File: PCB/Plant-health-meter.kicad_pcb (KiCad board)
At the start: 4 copper layers, 128 x 25 mm, 85 parts, among them J1 Conn_01x02, J2 Conn_01x02, J3 Conn_01x04, J4 UJ2-MIBH2-4-SMT-TR, J5 Conn_01x02, Q1 AO3401A, SW1 Boot, SW2 Reset, U1 LTC4412xS6, U2 TPS62172DSG, U3 USBLC6-2P6, U4 ESP32-C3FH4X, U5 BME280, U6 TPS61022, U8 TP4057, U9 TLC555xD, Y1 40MHz

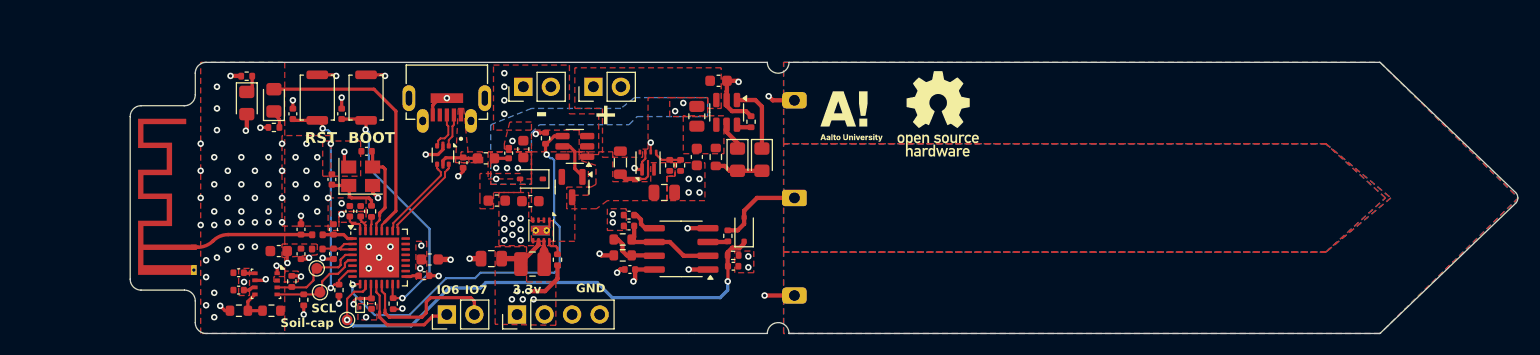
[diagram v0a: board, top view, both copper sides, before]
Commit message: Added light sensor simulation and schematic
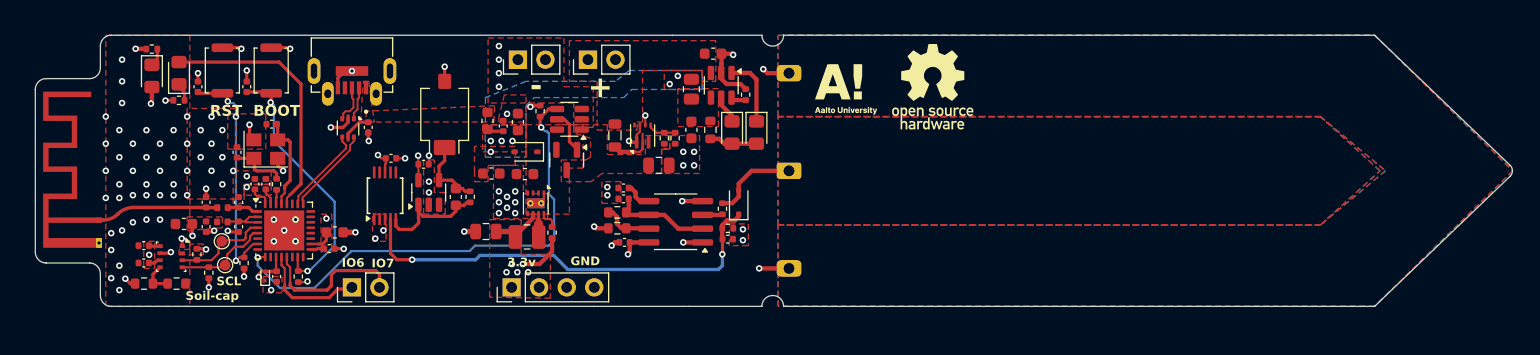
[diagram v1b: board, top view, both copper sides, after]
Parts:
- removed TP3: TestPoint, TestPoint:TestPoint_Pad_D1.0mm
- added C1: 100n, Capacitor_SMD:C_0402_1005Metric, F.Cu at (118.0, 108.8)
- added C30: 1u, Capacitor_SMD:C_0603_1608Metric, F.Cu at (124.0, 112.4)
- added C31: 100n, Capacitor_SMD:C_0402_1005Metric, F.Cu at (121.0, 109.4)
- added D7: BPW34-SMD, OptoDevice:Osram_BPW34S-SMD, F.Cu at (123.0, 104.8)
- added R21: 33k, Resistor_SMD:R_0402_1005Metric, F.Cu at (125.3, 112.4)
- added U12: ADS1115IDGS, Package_SO:TSSOP-10_3x3mm_P0.5mm, F.Cu at (117.5, 112.3)
- added U7: OPA340NA, Package_TO_SOT_SMD:SOT-23-5, F.Cu at (121.5, 112.0)
- moved C3 9.33 mm to (116.0, 106.0)
- moved AE1 9.10 mm to (91.1, 114.5)
- moved C10 9.10 mm to (99.0, 114.9)
- moved C11 9.10 mm to (101.0, 115.2)
- moved C12 9.10 mm to (104.0, 115.2)
- moved C13 9.10 mm to (112.3, 117.2)
- moved C14 9.10 mm to (112.9, 115.7)
- moved C15 9.10 mm to (104.0, 112.9)
- moved C16 9.10 mm to (107.5, 119.8)
- moved C17 9.10 mm to (101.0, 112.9)
- moved C18 9.10 mm to (105.5, 111.2)
- moved C19 9.10 mm to (106.5, 111.2)
- moved C20 9.10 mm to (100.2, 102.2)
- moved C21 9.10 mm to (95.2, 118.5)
- moved C22 9.10 mm to (95.2, 116.9)
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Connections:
- C26 pad 2: /MCU/Soil_cap -> /ADC/Soil_cap
- D8 pad 1: /MCU/Soil_cap -> /ADC/Soil_cap
- R17 pad 2: /MCU/Soil_cap -> /ADC/Soil_cap
- U4 pad 10: /MCU/Soil_cap -> unconnected-(U4-MTDI-Pad10)
- U4 pad 18: unconnected-(U4-VDD_SPI-Pad18) -> +3.3V
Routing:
- net /MCU/Soil_cap: track 47.9 -> 0.00 mm, vias 2 -> 0
- net /ADC/Soil_cap: track 0.00 -> 40.7 mm, vias 0 -> 2
- net /ADC/Light level: track 0.00 -> 11.2 mm
- net /MCU/Battery_stat: track 37.2 -> 45.4 mm
- net +3.3V: track 37.0 -> 43.8 mm, vias 22 -> 23
- net Net-(D7-K): track 0.00 -> 6.76 mm
- net GND: track 41.1 -> 44.0 mm, vias 101 -> 108
- net VBUS: track 3.72 -> 2.71 mm
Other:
- board size 128 x 25 mm -> 136.2 x 25 mm

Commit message: Light sensor
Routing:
- net Net-(D7-K): track 6.76 -> 4.82 mm
- net GND: track 44.0 -> 42.6 mm, vias 108 -> 107
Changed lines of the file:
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@@
 			(outputformat 1)
 			(mirror no)
-			(drillshape 1)
+			(drillshape 0)
 			(scaleselection 1)
-			(outputdirectory "")
+			(outputdirectory "manufacture/")
 		)
 	)
@@
 		(tags "capacitor")
 		(property "Reference" "C31"
-			(at 0 -1.16 360)
+			(at 0 -1.16 0)
 			(layer "F.SilkS")
 			(hide yes)
@@
 		)
 		(property "Value" "100n"
-			(at 0 1.16 360)
+			(at 0 1.16 0)
 			(layer "F.Fab")
 			(effects
@@
 		)
 		(fp_text user "${REFERENCE}"
-			(at 0 0 360)
+			(at 0 0 0)
 			(layer "F.Fab")
 			(effects
@@
 		(tags "capacitor")
 		(property "Reference" "C1"
-			(at 0 -1.16 360)
+			(at 0 -1.16 0)
 			(layer "F.SilkS")
 			(hide yes)
@@
 		)
 		(property "Value" "100n"
-			(at 0 1.16 360)
+			(at 0 1.16 0)
 			(layer "F.Fab")
 			(effects
@@
 		)
 		(fp_text user "${REFERENCE}"
-			(at 0 0 360)
+			(at 0 0 0)
 			(layer "F.Fab")
 			(effects
@@
 	)
 	(segment
-		(start 123 101.75)
-		(end 123 100.4)
-		(width 0.3)
-		(layer "F.Cu")
-		(net 2)
-	)
-	(segment
 		(start 115.95 106.48)
 		(end 115.95 107.2)
@@
 	)
 	(via
-		(at 123 100.4)
-		(size 0.6)
-		(drill 0.3)
-		(layers "F.Cu" "B.Cu")
-		(net 2)
-	)
-	(via
 		(at 91.75 110)
 		(size 0.6)
@@
 	)
 	(segment
-		(start 122.479999 109.57)
-		(end 123 109.049999)
-		(width 0.3)
-		(layer "F.Cu")
-		(net 57)
-	)
-	(segment
 		(start 124.6325 111.6325)
 		(end 124.029999 111.6325)
@@
 		(width 0.3)
 		(layer "F.Cu")
-		(net 57)
-	)
-	(segment
-		(start 123 109.049999)
-		(end 123 107.85)
-		(width 0.3)
-		(layer "F.Cu")

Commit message: Cleaned up
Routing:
- net Net-(D7-K): track 4.82 -> 6.76 mm
- net GND: track 42.6 -> 44.1 mm, vias 107 -> 108
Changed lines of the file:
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@@
 	)
 	(segment
+		(start 123 101.75)
+		(end 123 100.25)
+		(width 0.3)
+		(layer "F.Cu")
+		(net 2)
+	)
+	(segment
 		(start 138.69 116.6)
 		(end 138.3975 116.8925)
@@
 	)
 	(via
+		(at 123 100.25)
+		(size 0.6)
+		(drill 0.3)
+		(layers "F.Cu" "B.Cu")
+		(net 2)
+	)
+	(via
 		(at 94.5 98.75)
 		(size 0.6)
@@
 	)
 	(segment
-		(start 124.89 111.89)
-		(end 124.6325 111.6325)
+		(start 122.479999 109.520001)
+		(end 123 109)
 		(width 0.3)
 		(layer "F.Cu")
@@
 	)
 	(segment
-		(start 124.029999 111.229999)
-		(end 124.029999 111.6325)
+		(start 123 109)
+		(end 123 107.85)
 		(width 0.3)
 		(layer "F.Cu")
@@
 	(segment
 		(start 122.479999 110.8625)
-		(end 122.479999 109.57)
+		(end 122.479999 109.520001)
+		(width 0.3)
+		(layer "F.Cu")
+		(net 57)
+	)
+	(segment
+		(start 124.89 111.89)
+		(end 124.6325 111.6325)
+		(width 0.3)
+		(layer "F.Cu")
+		(net 57)
+	)
+	(segment
+		(start 124.029999 111.229999)
+		(end 124.029999 111.6325)
 		(width 0.3)
 		(layer "F.Cu")

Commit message: removed usb port library
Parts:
- C15, C17: value 3.3p -> 2.2p
- C8, C9: value 9p -> 22p
- L4: value 2.2n -> 2.6n
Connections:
- R8 pad 2: /MCU/SDA -> /ADC/SDA
- R9 pad 2: /MCU/SCL -> /ADC/SCL
- TP1 pad 1: /MCU/SDA -> /ADC/SDA
- TP2 pad 1: /MCU/SCL -> /ADC/SCL
- U4 pad 4: /MCU/SDA -> /ADC/SDA
- U4 pad 5: /MCU/SCL -> /ADC/SCL
- U5 pad 3: /MCU/SDA -> /ADC/SDA
- U5 pad 4: /MCU/SCL -> /ADC/SCL
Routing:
- net /MCU/SDA: track 8.95 -> 0.00 mm
- net /ADC/SDA: track 0.00 -> 8.95 mm
- net /MCU/SCL: track 8.86 -> 0.00 mm
- net /ADC/SCL: track 0.00 -> 8.86 mm

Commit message: latest
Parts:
- removed J4: UJ2-MIBH2-4-SMT-TR, UJ2-MIBH2-4-SMT-TR:CUI_UJ2-MIBH2-4-SMT-TR
- added J6: USB_B_Micro, Connector_USB:USB_Micro-B_Molex-105017-0001, F.Cu at (114.5, 101.1)
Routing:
- net /ADC/SDA: track 8.95 -> 18.1 mm, vias 0 -> 1
- net /ADC/SCL: track 8.86 -> 16.6 mm, vias 0 -> 1
- net GND: track 44.1 -> 41.7 mm, vias 108 -> 107
- net /PWR/D+: track 3.56 -> 2.47 mm
- net /PWR/D-: track 3.05 -> 1.96 mm

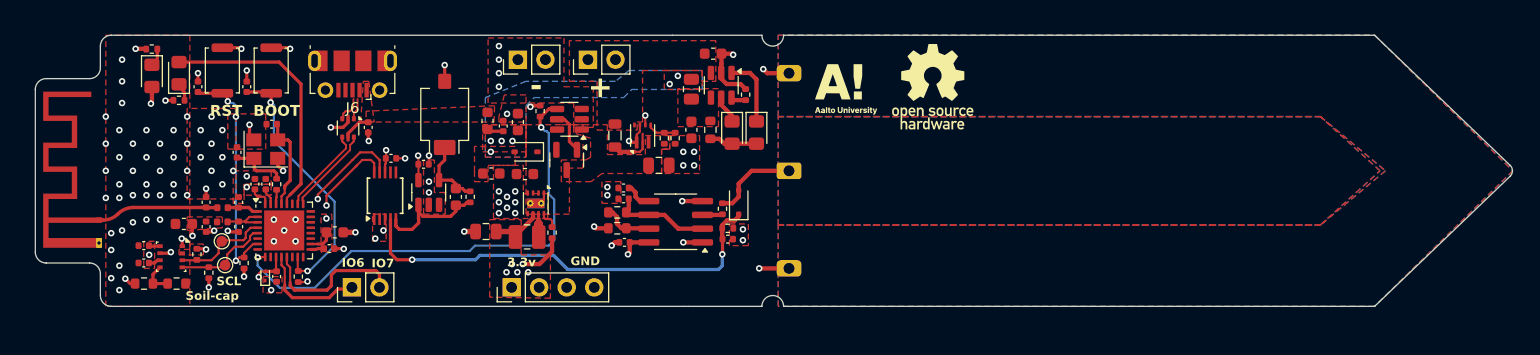
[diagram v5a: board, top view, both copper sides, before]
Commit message: Optimized PCB lauout and added Header for LED indicator bar
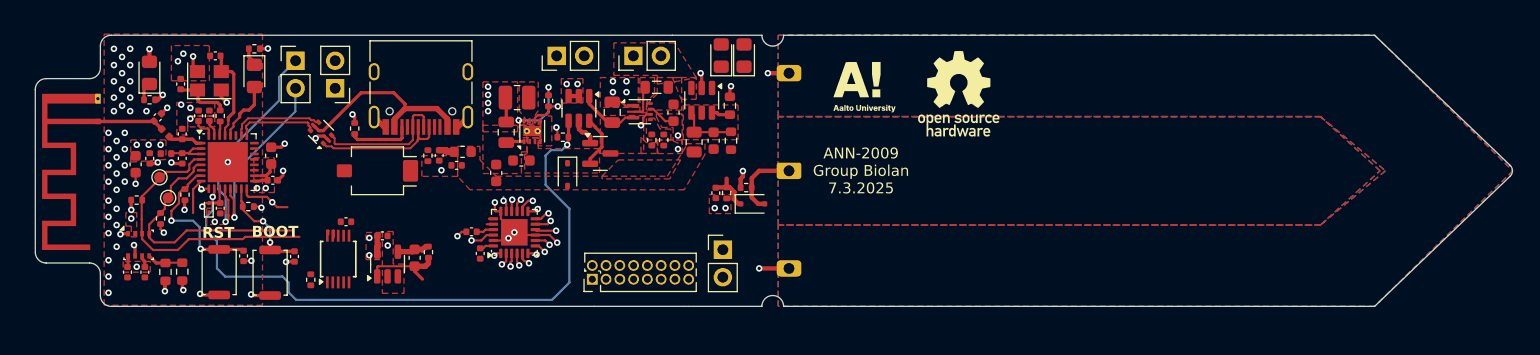
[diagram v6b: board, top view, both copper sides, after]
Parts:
- removed C25: 1n, Capacitor_SMD:C_0402_1005Metric
- removed the C5 at (127.3, 110.2)
- removed J3: Conn_01x04, Connector_PinHeader_2.54mm:PinHeader_1x04_P2.54mm_Vertical
- removed R16: 1.6k, Resistor_SMD:R_0603_1608Metric
- added J4: USB_C_Receptacle_USB2.0_14P, Connector_USB:USB_C_Receptacle_HRO_TYPE-C-31-M-12, F.Cu at (120.8, 101.9)
- added J7: Conn_01x02, Connector_PinHeader_2.54mm:PinHeader_1x02_P2.54mm_Vertical, F.Cu at (112.9, 102.4)
- added J8: Conn_01x02, Connector_PinHeader_2.54mm:PinHeader_1x02_P2.54mm_Vertical, F.Cu at (148.7, 117.3)
- added R22: 5.1k, Resistor_SMD:R_0402_1005Metric, F.Cu at (114.7, 106.1)
- added R23: 5.1k, Resistor_SMD:R_0402_1005Metric, F.Cu at (121.5, 108.6)
- AE1: footprint RF_Antenna:Texas_SWRA117D_2.4GHz_Right -> RF_Antenna:Texas_SWRA117D_2.4GHz_Left
- C23: value 10n -> 100n
- J6: value USB_B_Micro -> Conn_02x08_Counter_Clockwise; footprint Connector_USB:USB_Micro-B_Molex-105017-0001 -> Connector_PinHeader_1.27mm:PinHeader_2x08_P1.27mm_Vertical
- L1: value 2.2n -> 1u
- R14: value 330 -> 4.7k; footprint Resistor_SMD:R_0603_1608Metric -> Resistor_SMD:R_0402_1005Metric
- R19: value 10k -> 5.1k; footprint Resistor_SMD:R_0402_1005Metric -> Resistor_SMD:R_0603_1608Metric
- U9: value TLC555xD -> TCA9555RTWR; footprint Package_SO:SOIC-8_3.9x4.9mm_P1.27mm -> Package_DFN_QFN:WQFN-24-1EP_4x4mm_P0.5mm_EP2.45x2.45mm
- moved J6 29.1 mm to (136.6, 120.0), turned to 90 degrees
- moved R14 28.7 mm to (110.7, 120.0), turned to -90 degrees
- moved J5 21.5 mm to (109.2, 99.8), turned to 0 degrees
- moved SW1 18.7 mm to (106.9, 119.4), turned to -90 degrees
- moved SW2 18.6 mm to (102.2, 119.3), turned to -90 degrees
- moved C7 16.3 mm to (109.2, 117.9), turned to 90 degrees
- moved C20 16.2 mm to (104.5, 117.8), turned to -90 degrees
- moved U9 14.9 mm to (129.4, 115.7), turned to 90 degrees
- moved C23 14.6 mm to (125.5, 115.6)
- moved C24 13.3 mm to (126.3, 117.6), turned to -90 degrees
- moved L2 12.9 mm to (129.7, 103.2)
- moved R4 12.2 mm to (132.6, 103.6)
- moved C6 9.34 mm to (128.7, 106.5), turned to -90 degrees
- moved C14 9.19 mm to (107.0, 108.6), turned to 90 degrees
- moved AE1 9.10 mm to (91.0, 105.5)
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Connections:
- net /MCU/DEBUG renamed /ESP_32/DEBUG
- net /MCU/USB_D+ renamed /ESP_32/USB_D+
- net /MCU/USB_D- renamed /ESP_32/USB_D-
- net Net-(U2-SW) renamed /PWR/Buck_ind
- net Net-(U6-FB) renamed /PWR/Boost_VD
- net Net-(U6-SW) renamed /PWR/Boost_Ind
- C23 pad 1: Net-(U9-CV) -> +3.3V
- J6 pad 1: VBUS -> Net-(J6-Pin_1)
- J6 pad 2: /PWR/D- -> Net-(J6-Pin_2)
- J6 pad 3: /PWR/D+ -> Net-(J6-Pin_3)
- J6 pad 4: unconnected-(J6-ID-Pad4) -> Net-(J6-Pin_4)
- J6 pad 5: GND -> Net-(J6-Pin_5)
- J6 pad 6: GND -> Net-(J6-Pin_6)
- R1 pad 2: /MCU/Battery_stat -> /ESP_32/Battery_stat
- R14 pad 1: Net-(U9-DIS) -> +3.3V
- R14 pad 2: +3.3V -> /ADC/ALERT
- R15 pad 1: /Sensors/Q -> /ESP_32/SOIL_PWM
- R20 pad 1: +5V -> /PWR/charge
- R20 pad 2: /PWR/charge -> +5V
- U1 pad 4: /MCU/Battery_stat -> /ESP_32/Battery_stat
- U12 pad 6: unconnected-(U12-AIN2-Pad6) -> +BATT
- U4 pad 10: unconnected-(U4-MTDI-Pad10) -> /ESP_32/Battery_stat
- U4 pad 16: unconnected-(U4-GPIO10-Pad16) -> /ESP_32/IO_INT
- U4 pad 8: unconnected-(U4-GPIO3-Pad8) -> /ADC/ALERT
- U4 pad 9: /MCU/Battery_stat -> /ESP_32/SOIL_PWM
- U9 pad 1: GND -> Net-(J6-Pin_1)
- U9 pad 2: Net-(U9-THR) -> Net-(J6-Pin_2)
- U9 pad 3: /Sensors/Q -> Net-(J6-Pin_3)
- U9 pad 4: +3.3V -> Net-(J6-Pin_4)
- U9 pad 5: Net-(U9-CV) -> Net-(J6-Pin_5)
- U9 pad 6: Net-(U9-THR) -> Net-(J6-Pin_6)
- U9 pad 7: Net-(U9-DIS) -> Net-(J6-Pin_7)
- U9 pad 8: +3.3V -> Net-(J6-Pin_8)
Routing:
- net /ESP_32/Battery_stat: track 0.00 -> 60.3 mm, vias 0 -> 2
- net /MCU/Battery_stat: track 45.4 -> 0.00 mm, vias 2 -> 0
- net /ADC/Soil_cap: track 40.7 -> 4.18 mm, vias 2 -> 0
- net /ESP_32/DEBUG: track 23.9 -> 5.73 mm
- net VBUS: track 2.71 -> 19.5 mm
- net Net-(U4-GPIO9): track 24.7 -> 9.45 mm
- net +3.3V: track 43.7 -> 30.5 mm, vias 23 -> 24
- net /PWR/D-: track 1.96 -> 13.5 mm
- net Net-(J5-Pin_1): track 10.1 -> 21.5 mm, vias 0 -> 1
- net /PWR/D+: track 2.47 -> 12.5 mm
- net GND: track 41.7 -> 51.7 mm, vias 107 -> 82
- net /ADC/SDA: track 18.1 -> 27.8 mm, vias 1 -> 0
- net Net-(U9-THR): track 9.00 -> 0.00 mm
- net /ADC/SCL: track 16.6 -> 24.0 mm, vias 1 -> 0
- net /ESP_32/IO_INT: track 0.00 -> 7.03 mm, vias 0 -> 2
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- added copper zone on F.Cu, net /PWR/Boost_Ind
- added copper zone on F.Cu, net /PWR/Boost_VD
- added copper zone on F.Cu, net /PWR/Buck_ind
- removed copper zone on B.Cu, net +5V
- removed copper zone on F.Cu, net VBUS
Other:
- board text added: "ANN-2009 Group Biolan 7.3.2025"
- board text removed: "+"
- board text removed: "-"
- board text removed: "3.3v"
- board text removed: "GND"
- board text removed: "IO6"
- board text removed: "IO7"
- board text removed: "SCL"
- board text removed: "Soil-cap"

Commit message: Finished PCB routing and added reference designators
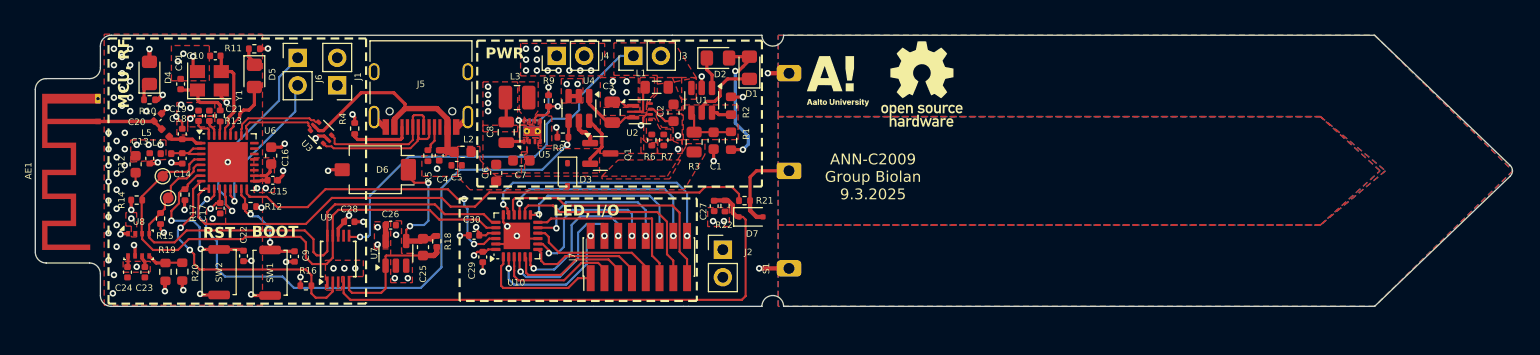
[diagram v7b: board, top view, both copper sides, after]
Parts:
- removed the D3 at (101.2, 113.4)
- J7: renamed from J6; footprint Connector_PinHeader_1.27mm:PinHeader_2x08_P1.27mm_Vertical -> Connector_PinHeader_1.27mm:PinHeader_2x08_P1.27mm_Vertical_SMD
- moved J7 4.76 mm to (140.9, 118.0)
- moved G*** 3.52 mm to (167.0, 102.0)
- moved G*** 2.51 mm to (159.2, 101.8)
- moved R18 1.25 mm to (122.3, 116.5)
- moved C25 1.25 mm to (121.0, 117.0)
- moved C26 1.25 mm to (118.0, 115.0)
- moved U7 1.25 mm to (118.5, 117.6)
- moved D1 1.23 mm to (151.1, 100.5)
- moved C27 1.21 mm to (147.9, 113.2)
- moved D7 1.21 mm to (151.2, 114.2)
- moved R21 1.21 mm to (150.7, 112.7)
- moved R22 1.21 mm to (148.9, 113.2)
- moved R16 0.71 mm to (110.2, 120.6), turned to 0 degrees
- moved C30 0.40 mm to (125.7, 116.0)
- moved C29 0.40 mm to (126.5, 118.0)
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- renumbered C29 to C1, C8 to C10, C9 to C11, C10 to C12, C11 to C13, C12 to C14, C13 to C15, C14 to C16, C16 to C17, C15 to C18, C18 to C19, C27 to C2, C17 to C20, C19 to C21, C20 to C22, C21 to C23, C22 to C24, C30 to C25, C31 to C26, C26 to C27, C1 to C28, C24 to C29, C28 to C3, C23 to C30, C3 to C4, C4 to C5, C5 to C6, C2 to C7, C6 to C8, C7 to C9, D6 to D1, D1 to D2, D5 to D3, D2 to D4, D4 to D5, D7 to D6, D8 to D7, J7 to J1, J8 to J2, J1 to J3, J2 to J4, J4 to J5, J5 to J6, L5 to L1, L1 to L2, L2 to L3, L3 to L4, L4 to L5, R18 to R1, R5 to R10, R10 to R11, R6 to R12, R7 to R13, R8 to R14, R9 to R15, R14 to R16, R11 to R17, R21 to R18, R12 to R19, R19 to R2, R13 to R20, R15 to R21, R17 to R22, R20 to R3, R22 to R4, R23 to R5, R2 to R6, R3 to R7, R1 to R8, R4 to R9, U8 to U1, U9 to U10, U6 to U2, U1 to U4, U2 to U5, U4 to U6, U5 to U8, U12 to U9
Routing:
- net /ESP_32/SOIL_PWM: track 2.42 -> 56.4 mm, vias 2 -> 0
- net /ADC/Soil_cap: track 4.18 -> 49.7 mm
- net +BATT: track 0.00 -> 37.1 mm, vias 0 -> 1
- net /ADC/SCL: track 24.0 -> 48.4 mm
- net /ADC/SDA: track 27.8 -> 51.6 mm
- net Net-(J7-Pin_16): track 1.38 -> 23.9 mm, vias 1 -> 2
- net Net-(J7-Pin_15): track 1.28 -> 23.7 mm, vias 1 -> 0
- net /ADC/ALERT: track 3.31 -> 25.3 mm, vias 0 -> 2
- net /ESP_32/IO_INT: track 7.03 -> 28.8 mm
- net Net-(J7-Pin_14): track 1.60 -> 19.9 mm, vias 1 -> 2
- net Net-(J7-Pin_13): track 1.61 -> 19.8 mm, vias 1 -> 0
- net Net-(J7-Pin_12): track 1.27 -> 16.3 mm, vias 1 -> 2
- net Net-(J7-Pin_11): track 1.42 -> 16.4 mm, vias 1 -> 0
- net Net-(J7-Pin_8): track 1.48 -> 14.6 mm, vias 1 -> 2
- net Net-(D1-A): track 0.00 -> 13.0 mm, vias 0 -> 2
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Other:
- board text added: "ANN-C2009 Group Biolan 9.3.2025"
- board text added: "LED, I/O"
- board text added: "MCU, RF"
- board text added: "PWR"
- board text removed: "ANN-2009 Group Biolan 7.3.2025"

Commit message: Final touches to PCB
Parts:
- removed the G*** at (167.0, 102.0)
- added C27: 100n, Capacitor_SMD:C_0402_1005Metric, F.Cu at (123.0, 119.6)
- added C29: 100n, Capacitor_SMD:C_0402_1005Metric, F.Cu at (151.0, 118.3)
- added G***: LOGO, LOGO, F.Cu at (166.8, 101.6)
- added G***: LOGO, LOGO, B.Cu at (137.8, 110.1)
- added R19: 500, Resistor_SMD:R_0402_1005Metric, F.Cu at (122.0, 119.6)
- added R24: 500, Resistor_SMD:R_0402_1005Metric, F.Cu at (151.0, 116.4)
- added R25: 10k, Resistor_SMD:R_0402_1005Metric, F.Cu at (116.7, 116.6)
- added R26: 10k, Resistor_SMD:R_0402_1005Metric, F.Cu at (115.7, 116.6)
- added TP3: TestPoint, TestPoint:TestPoint_Pad_D1.0mm, F.Cu at (124.5, 120.1)
- added TP4: TestPoint, TestPoint:TestPoint_Pad_D1.0mm, F.Cu at (126.1, 121.4)
- C25: value 1u -> 500n
- L2: footprint Inductor_SMD:L_0603_1608Metric -> Inductor_SMD:L_0805_2012Metric
- moved R10 4.66 mm to (95.5, 98.8), turned to 180 degrees
- moved C25 1.05 mm to (122.1, 117.0)
- moved C26 1.05 mm to (119.1, 115.0)
- moved R18 1.05 mm to (123.3, 116.5)
- moved U7 1.05 mm to (119.6, 117.6)
- moved C28 0.85 mm to (147.0, 113.2)
- moved D7 0.85 mm to (150.4, 114.2)
- moved R22 0.85 mm to (149.8, 112.7)
- moved R23 0.85 mm to (148.0, 113.2)
- moved J1 0.65 mm to (113.1, 102.8)
- moved J6 0.62 mm to (109.4, 100.2)
- moved G*** 0.57 mm to (159.8, 101.6)
- moved D4 0.41 mm to (95.5, 101.3), turned to -90 degrees
- moved D6 0.30 mm to (116.6, 110.2)
- moved J5 0.21 mm to (120.8, 101.7)
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- renumbered C27 to C28, C28 to C30, C29 to C31, C30 to C32, R19 to R20, R20 to R21, R21 to R22, R22 to R23
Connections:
- C25 pad 2: /ADC/Light level -> /Sensors/V_out
- C28 pad 2: /ADC/Soil_cap -> Net-(D7-K)
- D7 pad 1: /ADC/Soil_cap -> Net-(D7-K)
- R18 pad 2: /ADC/Light level -> /Sensors/V_out
- R23 pad 2: /ADC/Soil_cap -> Net-(D7-K)
- U7 pad 1: /ADC/Light level -> /Sensors/V_out
- U9 pad 6: +BATT -> Net-(U9-AIN2)
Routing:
- net /Sensors/V_out: track 0.00 -> 7.53 mm
- net /ADC/Soil_cap: track 49.7 -> 43.2 mm
- net Net-(D7-K): track 0.00 -> 6.03 mm
- net GND: track 51.7 -> 56.6 mm, vias 101 -> 114
- net /PWR/D+: track 12.5 -> 17.1 mm
- net Net-(U9-AIN2): track 0.00 -> 3.00 mm
- net +BATT: track 37.1 -> 35.2 mm
- net Net-(U6-GPIO9): track 9.46 -> 11.3 mm
- net Net-(D6-K): track 12.7 -> 11.3 mm
- net /ESP_32/SOIL_PWM: track 56.4 -> 55.1 mm
- net /ESP_32/USB_D-: track 7.56 -> 8.47 mm
- net VBUS: track 21.8 -> 22.6 mm
- net Net-(D4-K): track 1.67 -> 0.98 mm
- net /ADC/Light level: track 12.7 -> 12.0 mm
- net /Sensors/sensor_cap: track 8.34 -> 9.01 mm
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- added copper zone on F.Cu, net VBUS
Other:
- outline, holes or cut-outs redrawn
- board text added: "3v3"
- board text added: "GND"
- board text added: "IO21"
- board text added: "IO6"
- board text added: "IO7"
- board text added: "Light"
- board text added: "Soil"
- board text removed: "MCU, RF"
